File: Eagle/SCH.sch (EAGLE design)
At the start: 22 parts, among them Q1 IRF540, Q2 IRF540, Q3 IRF540, U1 ARDUINO-NANO

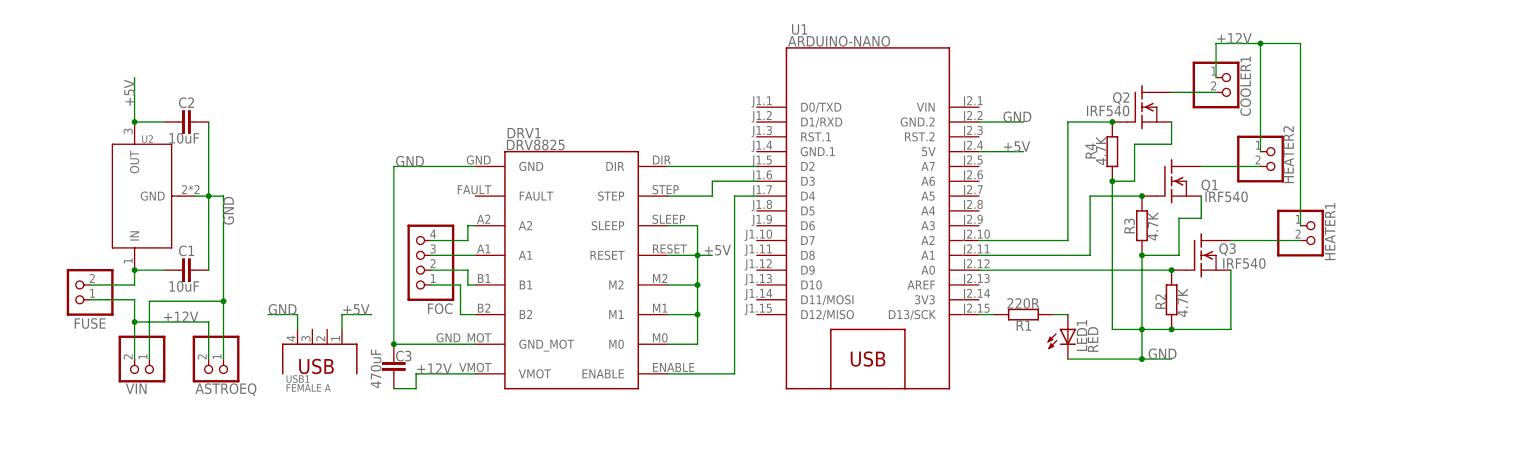
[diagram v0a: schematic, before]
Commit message: Added photos, Arduino SW update
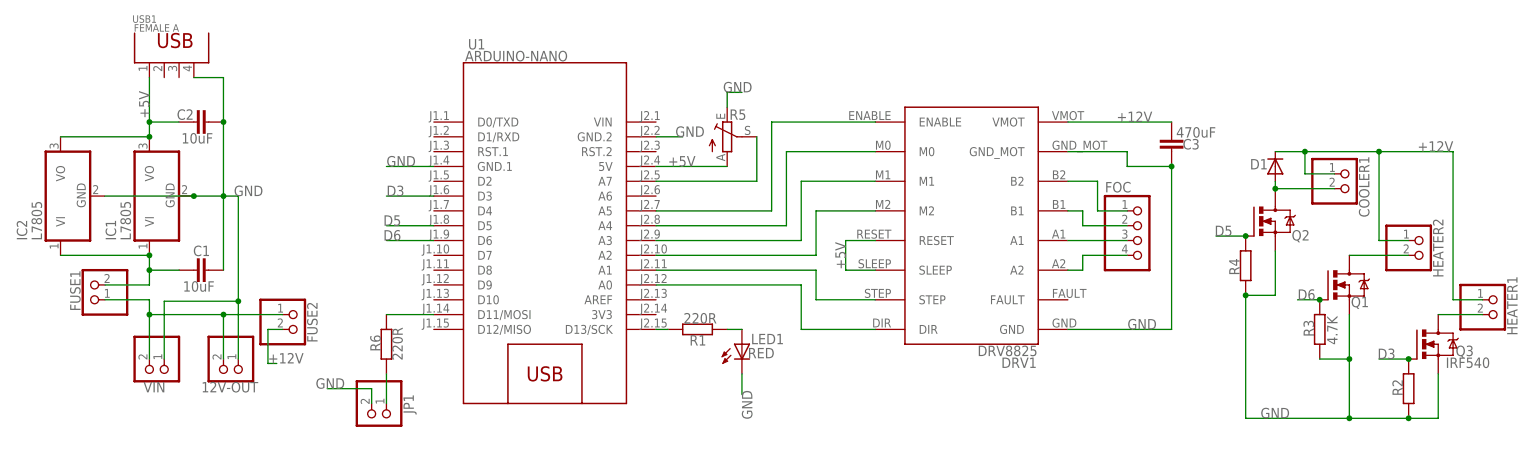
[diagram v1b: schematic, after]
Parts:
- removed ASTROEQ, FUSE: (no value), pinhead:PINHD-1X2
- removed U2: (no value), Seeed-IC:PMIC-ST-L7805CV(TO-220)
- added 12V-OUT, FUSE1, FUSE2, JP1: (no value), pinhead:PINHD-1X2
- added D1: (no value), diode:DIODE-D-2.5
- added IC1, IC2: L7805, linear:786TV
- added R5: (no value), pot:TRIM_EU-B64Y
- added R6: 220R, resistor:R-EU_0204/5
- C3: SPICEPREFIX (none) -> C
- DRV1, U1: SPICEPREFIX (none) -> X
- FOC: SPICEPREFIX (none) -> E
- HEATER1: SPICEPREFIX (none) -> H
- LED1: device Adafruit:LED3MM -> adafruit:LED3MM; SPICEPREFIX (none) -> L
- Q1, Q2, Q3: device transistor-fet:IRF540 -> transistor-power:IRF540
- R1: SPICEPREFIX (none) -> R
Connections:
- net N$17 renamed D13
- removed net N$7: Q2.G, R4.2, U1.A2
- new net D3: Q3.G, R2.2, U1.D3
- new net D5: Q2.G, R4.2, U1.D5
- new net D6: Q1.G, R3.2, U1.D6
- new net N$17: DRV1.M2, U1.A2
- new net N$18: DRV1.M1, U1.A3
- new net N$19: JP1.1, R6.1
- new net N$20: DRV1.M0, U1.A4
- new net N$8: 12V-OUT.2, FUSE1.1, FUSE2.1, VIN.2
- net +12V: now also D1.C, FUSE2.2; no longer ASTROEQ.2, FUSE.1, VIN.2
- net +5V: now also IC1.VO, IC2.VO, R5.A; no longer DRV1.M0, DRV1.M1, DRV1.M2, U2.OUT
- net GND: now also 12V-OUT.1, IC1.GND, IC2.GND, JP1.2, R5.E, U1.GND.1; no longer ASTROEQ.1, U2.GND
- net N$12: now also DRV1.STEP, U1.A1; no longer DRV1.ENABLE, U1.D4
- net N$2: now also R5.S, U1.A7; no longer DRV1.DIR, U1.D2
- net N$3: now also R6.2, U1.D11/MOSI; no longer DRV1.STEP, U1.D3
- net N$4: now also FUSE1.2, IC1.VI, IC2.VI; no longer FUSE.2, U2.IN
- net N$5: now also DRV1.DIR; no longer Q3.G, R2.2
- net N$6: now also DRV1.ENABLE, U1.A5; no longer Q1.G, R3.2, U1.A1
- net N$9: now also D1.A
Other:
- moved on the sheet: C1, C2, C3, COOLER1, DRV1, FOC, HEATER1, HEATER2, LED1, R1, R2, R3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

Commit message: New PCB design
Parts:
- removed COOLER1, HEATER1, HEATER2: (no value), pinhead:PINHD-1X2
- removed U1: ARDUINO-NANO, DIY:ARDUINO-NANO-3.0
- added JP3, JP4, JP5: (no value), SparkFun-Connectors:CONN_025MM
- added U$1: NANO, Arduino-clone:NANO
- FUSE1: value (none) -> 1.5A; device pinhead:PINHD-1X2 -> fuse:FUSEBLANK_5X20MM
- FUSE2: value (none) -> 2A; device pinhead:PINHD-1X2 -> fuse:FUSEBLANK_5X20MM
- JP2: value (none) -> FOCUSER
- VIN: device pinhead:PINHD-1X2 -> SparkFun-Connectors:CONN_025MM
- renumbered FOC to JP2
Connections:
- net +12V: now also JP3.1, JP4.1, JP5.1; no longer COOLER1.1, HEATER1.1, HEATER2.1
- net +5V: now also U$1.5.5V; no longer U1.5V
- net D13: now also U$1.D13; no longer U1.D13/SCK
- net D3: now also U$1.D3; no longer U1.D3
- net D5: now also U$1.D5; no longer U1.D5
- net D6: now also U$1.D6; no longer U1.D6
- net GND: now also U$1.GND, U$1.GND2; no longer U1.GND.1, U1.GND.2
- net N$10: now also JP4.2; no longer HEATER2.2
- net N$11: now also JP5.2; no longer HEATER1.2
- net N$12: now also U$1.A1; no longer U1.A1
- net N$17: now also U$1.A2; no longer U1.A2
- net N$18: now also U$1.A3; no longer U1.A3
- net N$2: now also U$1.A7; no longer U1.A7
- net N$20: now also U$1.A4; no longer U1.A4
- net N$3: now also U$1.D11; no longer U1.D11/MOSI
- net N$5: now also U$1.A0; no longer U1.A0
- net N$6: now also U$1.A5; no longer U1.A5
- net N$9: now also JP3.2; no longer COOLER1.2
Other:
- moved on the sheet: 12V-OUT, VIN
